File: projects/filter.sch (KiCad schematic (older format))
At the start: 24 parts, among them U601 OPA1632, U602 OPA1632

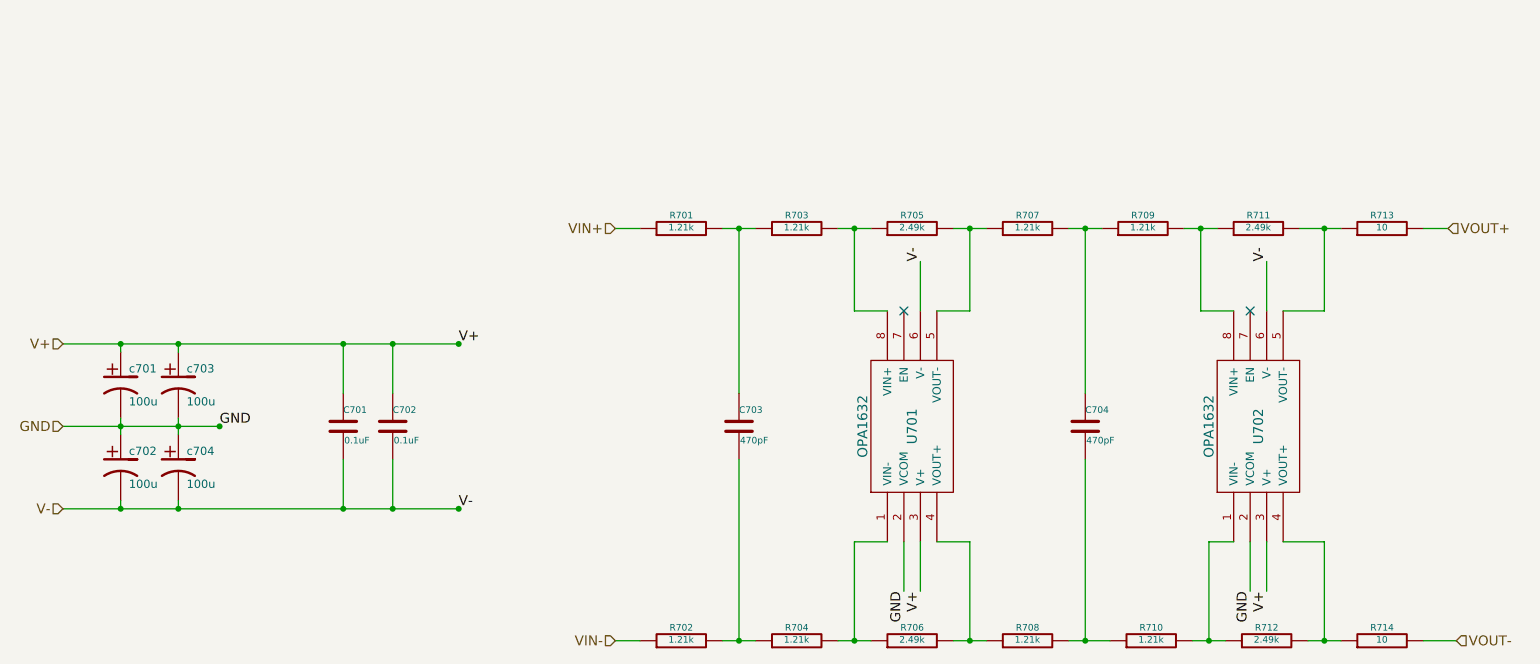
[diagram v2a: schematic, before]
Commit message: add connector footprints; change c_pol sch symbols
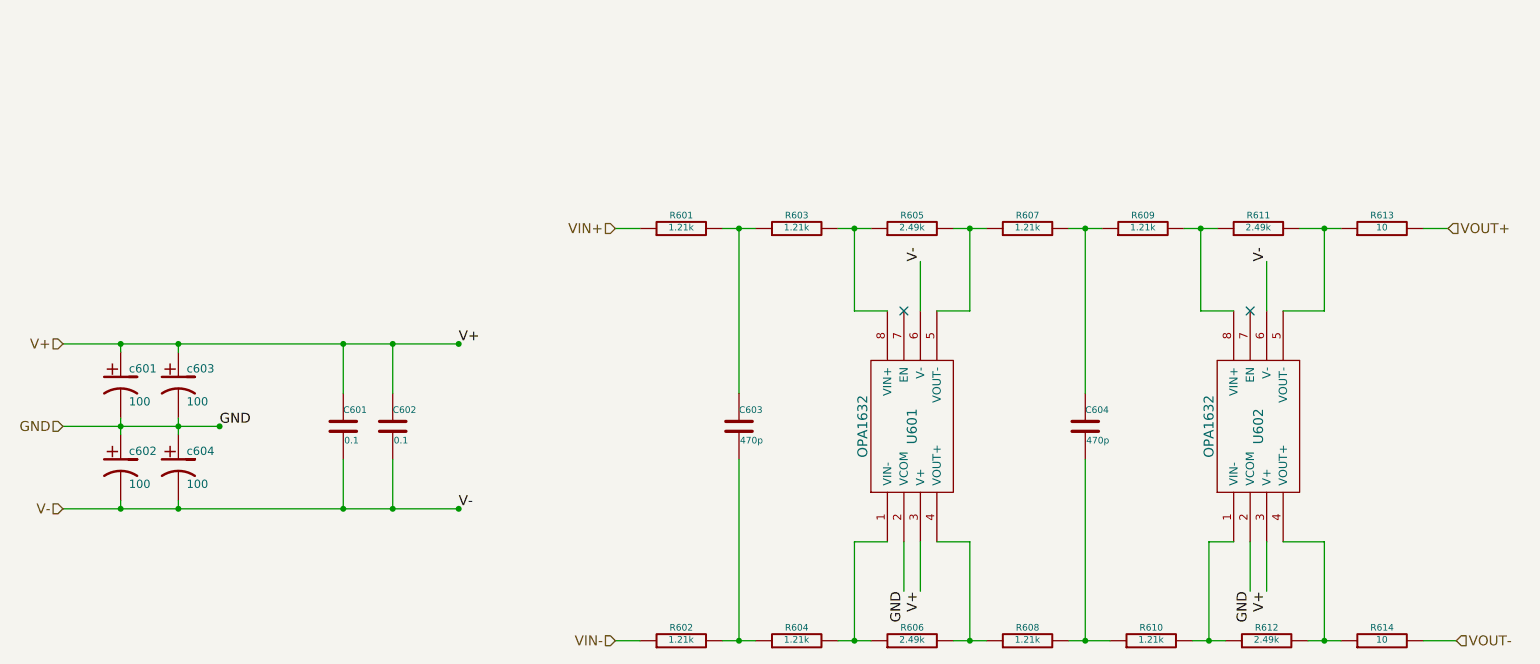
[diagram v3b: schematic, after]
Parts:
- C601, C602: value 0.1uF -> 0.1
- C603, C604: value 470pF -> 470p
- c601, c602, c603, c604: value 100u -> 100
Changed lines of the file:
@@
 AR Path="/541690F5/5428A511" Ref="C603"  Part="1"
 AR Path="/5428BABE/5428A511" Ref="C703"  Part="1"
-F 0 "C703" H 5850 4000 40  0000 L CNN
-F 1 "470pF" H 5856 3815 40  0000 L CNN
+F 0 "C603" H 5850 4000 40  0000 L CNN
+F 1 "470p" H 5856 3815 40  0000 L CNN
 F 2 "" H 5888 3750 30  0000 C CNN
 F 3 "" H 5850 3900 60  0000 C CNN
@@
 AR Path="/541690F5/5428A539" Ref="R601"  Part="1"
 AR Path="/5428BABE/5428A539" Ref="R701"  Part="1"
-F 0 "R701" V 5580 2700 40  0000 C CNN
+F 0 "R601" V 5580 2700 40  0000 C CNN
 F 1 "1.21k" V 5507 2701 40  0000 C CNN
 F 2 "" V 5430 2700 30  0000 C CNN
@@
 AR Path="/541690F5/5428B1BE" Ref="R605"  Part="1"
 AR Path="/5428BABE/5428B1BE" Ref="R705"  Part="1"
-F 0 "R705" V 6980 2700 40  0000 C CNN
+F 0 "R605" V 6980 2700 40  0000 C CNN
 F 1 "2.49k" V 6907 2701 40  0000 C CNN
 F 2 "" V 6830 2700 30  0000 C CNN
@@
 AR Path="/541690F5/5428B212" Ref="R613"  Part="1"
 AR Path="/5428BABE/5428B212" Ref="R713"  Part="1"
-F 0 "R713" V 9830 2700 40  0000 C CNN
+F 0 "R613" V 9830 2700 40  0000 C CNN
 F 1 "10" V 9757 2701 40  0000 C CNN
 F 2 "" V 9680 2700 30  0000 C CNN
@@
 AR Path="/541690F5/5431C69B" Ref="U601"  Part="1"
 AR Path="/5428BABE/5431C69B" Ref="U701"  Part="1"
-F 0 "U701" H 6900 3900 60  0000 C CNN
+F 0 "U601" H 6900 3900 60  0000 C CNN
 F 1 "OPA1632" H 6900 4200 60  0000 C CNN
 F 2 "" H 6900 3700 60  0000 C CNN
@@
 AR Path="/541690F5/5431C6F1" Ref="U602"  Part="1"
 AR Path="/5428BABE/5431C6F1" Ref="U702"  Part="1"
-F 0 "U702" H 9000 3900 60  0000 C CNN
+F 0 "U602" H 9000 3900 60  0000 C CNN
 F 1 "OPA1632" H 9000 4200 60  0000 C CNN
 F 2 "" H 9000 3700 60  0000 C CNN
@@
 AR Path="/541690F5/5431DA55" Ref="R603"  Part="1"
 AR Path="/5428BABE/5431DA55" Ref="R703"  Part="1"
-F 0 "R703" V 6280 2700 40  0000 C CNN
+F 0 "R603" V 6280 2700 40  0000 C CNN
 F 1 "1.21k" V 6207 2701 40  0000 C CNN
 F 2 "" V 6130 2700 30  0000 C CNN
@@
 AR Path="/541690F5/5431DA6A" Ref="R607"  Part="1"
 AR Path="/5428BABE/5431DA6A" Ref="R707"  Part="1"
-F 0 "R707" V 7680 2700 40  0000 C CNN
+F 0 "R607" V 7680 2700 40  0000 C CNN
 F 1 "1.21k" V 7607 2701 40  0000 C CNN
 F 2 "" V 7530 2700 30  0000 C CNN
@@
 AR Path="/541690F5/5431DA7F" Ref="R609"  Part="1"
 AR Path="/5428BABE/5431DA7F" Ref="R709"  Part="1"
-F 0 "R709" V 8380 2700 40  0000 C CNN
+F 0 "R609" V 8380 2700 40  0000 C CNN
 F 1 "1.21k" V 8307 2701 40  0000 C CNN
 F 2 "" V 8230 2700 30  0000 C CNN
@@
 AR Path="/541690F5/5431DA94" Ref="R611"  Part="1"
 AR Path="/5428BABE/5431DA94" Ref="R711"  Part="1"
-F 0 "R711" V 9080 2700 40  0000 C CNN
+F 0 "R611" V 9080 2700 40  0000 C CNN
 F 1 "2.49k" V 9007 2701 40  0000 C CNN
 F 2 "" V 8930 2700 30  0000 C CNN
@@
 AR Path="/541690F5/5431DAA9" Ref="R602"  Part="1"
 AR Path="/5428BABE/5431DAA9" Ref="R702"  Part="1"
-F 0 "R702" V 5580 5200 40  0000 C CNN
+F 0 "R602" V 5580 5200 40  0000 C CNN
 F 1 "1.21k" V 5507 5201 40  0000 C CNN
 F 2 "" V 5430 5200 30  0000 C CNN
@@
 AR Path="/541690F5/5431DABE" Ref="R604"  Part="1"
 AR Path="/5428BABE/5431DABE" Ref="R704"  Part="1"
-F 0 "R704" V 6280 5200 40  0000 C CNN
+F 0 "R604" V 6280 5200 40  0000 C CNN
 F 1 "1.21k" V 6207 5201 40  0000 C CNN
 F 2 "" V 6130 5200 30  0000 C CNN
@@
 AR Path="/541690F5/5431DB2C" Ref="R606"  Part="1"
 AR Path="/5428BABE/5431DB2C" Ref="R706"  Part="1"
-F 0 "R706" V 6980 5200 40  0000 C CNN
+F 0 "R606" V 6980 5200 40  0000 C CNN
 F 1 "2.49k" V 6907 5201 40  0000 C CNN
 F 2 "" V 6830 5200 30  0000 C CNN
@@
 AR Path="/541690F5/5431DB41" Ref="R608"  Part="1"
 AR Path="/5428BABE/5431DB41" Ref="R708"  Part="1"
-F 0 "R708" V 7680 5200 40  0000 C CNN
+F 0 "R608" V 7680 5200 40  0000 C CNN
 F 1 "1.21k" V 7607 5201 40  0000 C CNN
 F 2 "" V 7530 5200 30  0000 C CNN
@@
 AR Path="/541690F5/5431DB56" Ref="R610"  Part="1"
 AR Path="/5428BABE/5431DB56" Ref="R710"  Part="1"
-F 0 "R710" V 8430 5200 40  0000 C CNN
+F 0 "R610" V 8430 5200 40  0000 C CNN
 F 1 "1.21k" V 8357 5201 40  0000 C CNN
 F 2 "" V 8280 5200 30  0000 C CNN
@@
 AR Path="/541690F5/5431DB6B" Ref="R612"  Part="1"
 AR Path="/5428BABE/5431DB6B" Ref="R712"  Part="1"
-F 0 "R712" V 9130 5200 40  0000 C CNN
+F 0 "R612" V 9130 5200 40  0000 C CNN
 F 1 "2.49k" V 9057 5201 40  0000 C CNN
 F 2 "" V 8980 5200 30  0000 C CNN
@@
 AR Path="/541690F5/5431DDDC" Ref="C604"  Part="1"
 AR Path="/5428BABE/5431DDDC" Ref="C704"  Part="1"
-F 0 "C704" H 7950 4000 40  0000 L CNN
-F 1 "470pF" H 7956 3815 40  0000 L CNN
+F 0 "C604" H 7950 4000 40  0000 L CNN
+F 1 "470p" H 7956 3815 40  0000 L CNN
 F 2 "" H 7988 3750 30  0000 C CNN
 F 3 "" H 7950 3900 60  0000 C CNN
@@
 AR Path="/541690F5/5431E4D7" Ref="R614"  Part="1"
 AR Path="/5428BABE/5431E4D7" Ref="R714"  Part="1"
-F 0 "R714" V 9830 5200 40  0000 C CNN
+F 0 "R614" V 9830 5200 40  0000 C CNN
 F 1 "10" V 9757 5201 40  0000 C CNN
 F 2 "" V 9680 5200 30  0000 C CNN
@@
 AR Path="/541690F5/543A33EF" Ref="C601"  Part="1"
 AR Path="/5428BABE/543A33EF" Ref="C701"  Part="1"
-F 0 "C701" H 3450 4000 40  0000 L CNN
-F 1 "0.1uF" H 3456 3815 40  0000 L CNN
+F 0 "C601" H 3450 4000 40  0000 L CNN
+F 1 "0.1" H 3456 3815 40  0000 L CNN
 F 2 "" H 3488 3750 30  0000 C CNN
 F 3 "" H 3450 3900 60  0000 C CNN
@@
 AR Path="/541690F5/5449F9E9" Ref="C602"  Part="1"
 AR Path="/5428BABE/5449F9E9" Ref="C702"  Part="1"
-F 0 "C702" H 3750 4000 40  0000 L CNN
-F 1 "0.1uF" H 3756 3815 40  0000 L CNN
+F 0 "C602" H 3750 4000 40  0000 L CNN
+F 1 "0.1" H 3756 3815 40  0000 L CNN
 F 2 "" H 3788 3750 30  0000 C CNN
 F 3 "" H 3750 3900 60  0000 C CNN
@@
 AR Path="/541690F5/548575CB" Ref="c601"  Part="1"
 AR Path="/5428BABE/548575CB" Ref="c701"  Part="1"
-F 0 "c701" H 2150 3750 50  0000 L CNN
-F 1 "100u" H 2150 3550 50  0000 L CNN
+F 0 "c601" H 2150 3750 50  0000 L CNN
+F 1 "100" H 2150 3550 50  0000 L CNN
 F 2 "" H 2100 3650 60  0000 C CNN
 F 3 "" H 2100 3650 60  0000 C CNN
@@
 AR Path="/541690F5/54857740" Ref="c602"  Part="1"
 AR Path="/5428BABE/54857740" Ref="c702"  Part="1"
-F 0 "c702" H 2150 4250 50  0000 L CNN
-F 1 "100u" H 2150 4050 50  0000 L CNN
+F 0 "c602" H 2150 4250 50  0000 L CNN
+F 1 "100" H 2150 4050 50  0000 L CNN
 F 2 "" H 2100 4150 60  0000 C CNN
 F 3 "" H 2100 4150 60  0000 C CNN
@@
 AR Path="/541690F5/54857755" Ref="c603"  Part="1"
 AR Path="/5428BABE/54857755" Ref="c703"  Part="1"
-F 0 "c703" H 2500 3750 50  0000 L CNN
-F 1 "100u" H 2500 3550 50  0000 L CNN
+F 0 "c603" H 2500 3750 50  0000 L CNN
+F 1 "100" H 2500 3550 50  0000 L CNN
 F 2 "" H 2450 3650 60  0000 C CNN
 F 3 "" H 2450 3650 60  0000 C CNN
@@
 AR Path="/541690F5/5485776A" Ref="c604"  Part="1"
 AR Path="/5428BABE/5485776A" Ref="c704"  Part="1"
-F 0 "c704" H 2500 4250 50  0000 L CNN
-F 1 "100u" H 2500 4050 50  0000 L CNN
+F 0 "c604" H 2500 4250 50  0000 L CNN
+F 1 "100" H 2500 4050 50  0000 L CNN
 F 2 "" H 2450 4150 60  0000 C CNN
 F 3 "" H 2450 4150 60  0000 C CNN

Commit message: add equations into filter .sch sheets
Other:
- note added: "Fc = 1 / [2 x pi x 1.21 x 10^3 x (2x470) x 10^-12] = 139 KHz"
- note added: "Fc = 1 / [2 x pi x R x C]"
- note added: "Gain = (1/2) x 2 x (1/2) x 2 = 1"
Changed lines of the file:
@@
 	1    0    0    -1
 $EndComp
+Text Notes 6100 1500 0    60   ~ 0
+Gain = (1/2) x 2 x (1/2) x 2 = 1
+Text Notes 6200 1650 0    60   ~ 0
+Fc = 1 / [2 x pi x R x C]
+Text Notes 6200 1800 0    60   ~ 0
+Fc = 1 / [2 x pi x 1.21 x 10^3 x (2x470) x 10^-12] = 139 KHz
 $EndSCHEMATC

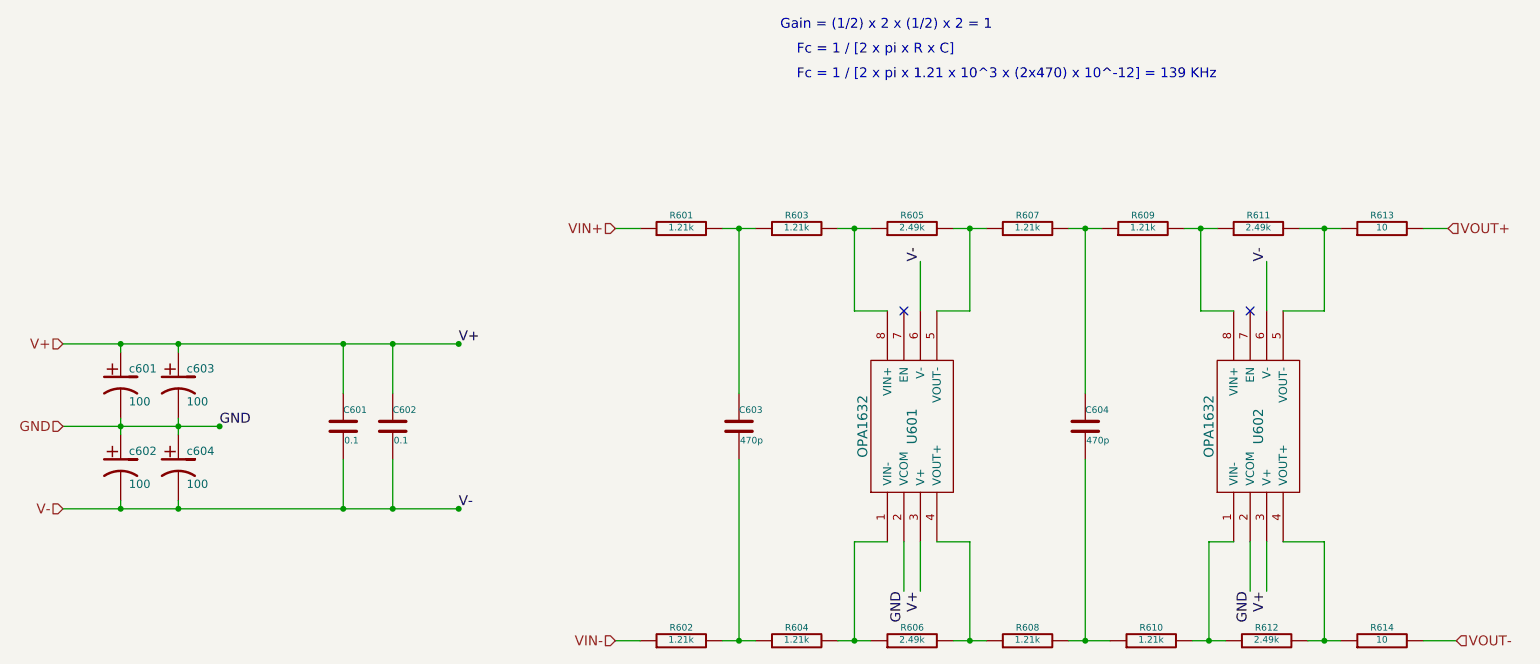
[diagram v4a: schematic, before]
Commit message: re-add netlist, correct part numbers
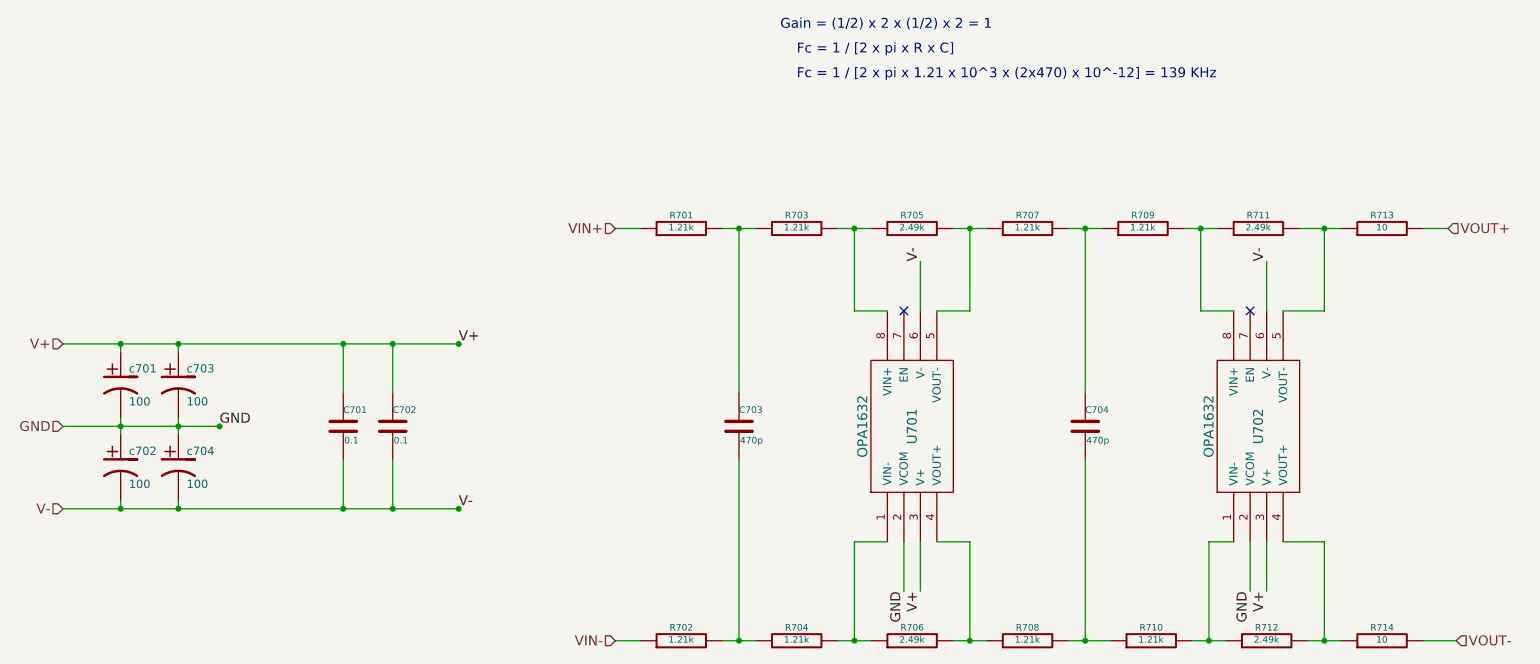
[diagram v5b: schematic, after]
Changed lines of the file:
@@
 LIBS:ti_gosselin
 LIBS:oscillator_gosselin
-LIBS:wolfson_gosselin
 LIBS:power
 LIBS:device
@@
 LIBS:linear_technology_gosselin
 LIBS:led_gosselin
-LIBS:mStereo2-cache
+LIBS:wolfson_gosselin
 EELAYER 24 0
 EELAYER END
 $Descr A4 11693 8268
 encoding utf-8
-Sheet 6 7
+Sheet 7 7
 Title ""
 Date ""
@@
 AR Path="/541690F5/5428A511" Ref="C603"  Part="1"
 AR Path="/5428BABE/5428A511" Ref="C703"  Part="1"
-F 0 "C603" H 5850 4000 40  0000 L CNN
+F 0 "C703" H 5850 4000 40  0000 L CNN
 F 1 "470p" H 5856 3815 40  0000 L CNN
 F 2 "" H 5888 3750 30  0000 C CNN
@@
 AR Path="/541690F5/5428A539" Ref="R601"  Part="1"
 AR Path="/5428BABE/5428A539" Ref="R701"  Part="1"
-F 0 "R601" V 5580 2700 40  0000 C CNN
+F 0 "R701" V 5580 2700 40  0000 C CNN
 F 1 "1.21k" V 5507 2701 40  0000 C CNN
 F 2 "" V 5430 2700 30  0000 C CNN
@@
 AR Path="/541690F5/5428B1BE" Ref="R605"  Part="1"
 AR Path="/5428BABE/5428B1BE" Ref="R705"  Part="1"
-F 0 "R605" V 6980 2700 40  0000 C CNN
+F 0 "R705" V 6980 2700 40  0000 C CNN
 F 1 "2.49k" V 6907 2701 40  0000 C CNN
 F 2 "" V 6830 2700 30  0000 C CNN
@@
 AR Path="/541690F5/5428B212" Ref="R613"  Part="1"
 AR Path="/5428BABE/5428B212" Ref="R713"  Part="1"
-F 0 "R613" V 9830 2700 40  0000 C CNN
+F 0 "R713" V 9830 2700 40  0000 C CNN
 F 1 "10" V 9757 2701 40  0000 C CNN
 F 2 "" V 9680 2700 30  0000 C CNN
@@
 AR Path="/541690F5/5431C69B" Ref="U601"  Part="1"
 AR Path="/5428BABE/5431C69B" Ref="U701"  Part="1"
-F 0 "U601" H 6900 3900 60  0000 C CNN
+F 0 "U701" H 6900 3900 60  0000 C CNN
 F 1 "OPA1632" H 6900 4200 60  0000 C CNN
 F 2 "" H 6900 3700 60  0000 C CNN
@@
 AR Path="/541690F5/5431C6F1" Ref="U602"  Part="1"
 AR Path="/5428BABE/5431C6F1" Ref="U702"  Part="1"
-F 0 "U602" H 9000 3900 60  0000 C CNN
+F 0 "U702" H 9000 3900 60  0000 C CNN
 F 1 "OPA1632" H 9000 4200 60  0000 C CNN
 F 2 "" H 9000 3700 60  0000 C CNN
@@
 AR Path="/541690F5/5431DA55" Ref="R603"  Part="1"
 AR Path="/5428BABE/5431DA55" Ref="R703"  Part="1"
-F 0 "R603" V 6280 2700 40  0000 C CNN
+F 0 "R703" V 6280 2700 40  0000 C CNN
 F 1 "1.21k" V 6207 2701 40  0000 C CNN
 F 2 "" V 6130 2700 30  0000 C CNN
@@
 AR Path="/541690F5/5431DA6A" Ref="R607"  Part="1"
 AR Path="/5428BABE/5431DA6A" Ref="R707"  Part="1"
-F 0 "R607" V 7680 2700 40  0000 C CNN
+F 0 "R707" V 7680 2700 40  0000 C CNN
 F 1 "1.21k" V 7607 2701 40  0000 C CNN
 F 2 "" V 7530 2700 30  0000 C CNN
@@
 AR Path="/541690F5/5431DA7F" Ref="R609"  Part="1"
 AR Path="/5428BABE/5431DA7F" Ref="R709"  Part="1"
-F 0 "R609" V 8380 2700 40  0000 C CNN
+F 0 "R709" V 8380 2700 40  0000 C CNN
 F 1 "1.21k" V 8307 2701 40  0000 C CNN
 F 2 "" V 8230 2700 30  0000 C CNN
@@
 AR Path="/541690F5/5431DA94" Ref="R611"  Part="1"
 AR Path="/5428BABE/5431DA94" Ref="R711"  Part="1"
-F 0 "R611" V 9080 2700 40  0000 C CNN
+F 0 "R711" V 9080 2700 40  0000 C CNN
 F 1 "2.49k" V 9007 2701 40  0000 C CNN
 F 2 "" V 8930 2700 30  0000 C CNN
@@
 AR Path="/541690F5/5431DAA9" Ref="R602"  Part="1"
 AR Path="/5428BABE/5431DAA9" Ref="R702"  Part="1"
-F 0 "R602" V 5580 5200 40  0000 C CNN
+F 0 "R702" V 5580 5200 40  0000 C CNN
 F 1 "1.21k" V 5507 5201 40  0000 C CNN
 F 2 "" V 5430 5200 30  0000 C CNN
@@
 AR Path="/541690F5/5431DABE" Ref="R604"  Part="1"
 AR Path="/5428BABE/5431DABE" Ref="R704"  Part="1"
-F 0 "R604" V 6280 5200 40  0000 C CNN
+F 0 "R704" V 6280 5200 40  0000 C CNN
 F 1 "1.21k" V 6207 5201 40  0000 C CNN
 F 2 "" V 6130 5200 30  0000 C CNN
@@
 AR Path="/541690F5/5431DB2C" Ref="R606"  Part="1"
 AR Path="/5428BABE/5431DB2C" Ref="R706"  Part="1"
-F 0 "R606" V 6980 5200 40  0000 C CNN
+F 0 "R706" V 6980 5200 40  0000 C CNN
 F 1 "2.49k" V 6907 5201 40  0000 C CNN
 F 2 "" V 6830 5200 30  0000 C CNN
@@
 AR Path="/541690F5/5431DB41" Ref="R608"  Part="1"
 AR Path="/5428BABE/5431DB41" Ref="R708"  Part="1"
-F 0 "R608" V 7680 5200 40  0000 C CNN
+F 0 "R708" V 7680 5200 40  0000 C CNN
 F 1 "1.21k" V 7607 5201 40  0000 C CNN
 F 2 "" V 7530 5200 30  0000 C CNN
@@
 AR Path="/541690F5/5431DB56" Ref="R610"  Part="1"
 AR Path="/5428BABE/5431DB56" Ref="R710"  Part="1"
-F 0 "R610" V 8430 5200 40  0000 C CNN
+F 0 "R710" V 8430 5200 40  0000 C CNN
 F 1 "1.21k" V 8357 5201 40  0000 C CNN
 F 2 "" V 8280 5200 30  0000 C CNN
@@
 AR Path="/541690F5/5431DB6B" Ref="R612"  Part="1"
 AR Path="/5428BABE/5431DB6B" Ref="R712"  Part="1"
-F 0 "R612" V 9130 5200 40  0000 C CNN
+F 0 "R712" V 9130 5200 40  0000 C CNN
 F 1 "2.49k" V 9057 5201 40  0000 C CNN
 F 2 "" V 8980 5200 30  0000 C CNN
@@
 AR Path="/541690F5/5431DDDC" Ref="C604"  Part="1"
 AR Path="/5428BABE/5431DDDC" Ref="C704"  Part="1"
-F 0 "C604" H 7950 4000 40  0000 L CNN
+F 0 "C704" H 7950 4000 40  0000 L CNN
 F 1 "470p" H 7956 3815 40  0000 L CNN
 F 2 "" H 7988 3750 30  0000 C CNN
@@
 AR Path="/541690F5/5431E4D7" Ref="R614"  Part="1"
 AR Path="/5428BABE/5431E4D7" Ref="R714"  Part="1"
-F 0 "R614" V 9830 5200 40  0000 C CNN
+F 0 "R714" V 9830 5200 40  0000 C CNN
 F 1 "10" V 9757 5201 40  0000 C CNN
 F 2 "" V 9680 5200 30  0000 C CNN
@@
 AR Path="/541690F5/543A33EF" Ref="C601"  Part="1"
 AR Path="/5428BABE/543A33EF" Ref="C701"  Part="1"
-F 0 "C601" H 3450 4000 40  0000 L CNN
+F 0 "C701" H 3450 4000 40  0000 L CNN
 F 1 "0.1" H 3456 3815 40  0000 L CNN
 F 2 "" H 3488 3750 30  0000 C CNN
@@
 AR Path="/541690F5/5449F9E9" Ref="C602"  Part="1"
 AR Path="/5428BABE/5449F9E9" Ref="C702"  Part="1"
-F 0 "C602" H 3750 4000 40  0000 L CNN
+F 0 "C702" H 3750 4000 40  0000 L CNN
 F 1 "0.1" H 3756 3815 40  0000 L CNN
 F 2 "" H 3788 3750 30  0000 C CNN
@@
 AR Path="/541690F5/548575CB" Ref="c601"  Part="1"
 AR Path="/5428BABE/548575CB" Ref="c701"  Part="1"
-F 0 "c601" H 2150 3750 50  0000 L CNN
+F 0 "c701" H 2150 3750 50  0000 L CNN
 F 1 "100" H 2150 3550 50  0000 L CNN
 F 2 "" H 2100 3650 60  0000 C CNN
@@
 AR Path="/541690F5/54857740" Ref="c602"  Part="1"
 AR Path="/5428BABE/54857740" Ref="c702"  Part="1"
-F 0 "c602" H 2150 4250 50  0000 L CNN
+F 0 "c702" H 2150 4250 50  0000 L CNN
 F 1 "100" H 2150 4050 50  0000 L CNN
 F 2 "" H 2100 4150 60  0000 C CNN
@@
 AR Path="/541690F5/54857755" Ref="c603"  Part="1"
 AR Path="/5428BABE/54857755" Ref="c703"  Part="1"
-F 0 "c603" H 2500 3750 50  0000 L CNN
+F 0 "c703" H 2500 3750 50  0000 L CNN
 F 1 "100" H 2500 3550 50  0000 L CNN
 F 2 "" H 2450 3650 60  0000 C CNN
@@
 AR Path="/541690F5/5485776A" Ref="c604"  Part="1"
 AR Path="/5428BABE/5485776A" Ref="c704"  Part="1"
-F 0 "c604" H 2500 4250 50  0000 L CNN
+F 0 "c704" H 2500 4250 50  0000 L CNN
 F 1 "100" H 2500 4050 50  0000 L CNN
 F 2 "" H 2450 4150 60  0000 C CNN
